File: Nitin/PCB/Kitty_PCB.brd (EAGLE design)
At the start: 384.8 x 406.1 mm, 49 parts

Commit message: PCB 1.0 Final
1st version of the PCB is completed.
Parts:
- removed C1: (no value), robocon:C050-075X075
- removed LED1, LED2, LED3, LED4, LED5: LED, robocon:LED3MM
- removed R3: (no value), robocon:0207/10
- added 5VLED, 9VLED, A1LED, A2LED: LED, robocon:LED3MM
- moved SCREW_TERMINAL2 378.1 mm to (19.1, 0.00), turned to 0 degrees
- moved SCREW_TERMINAL_1 346.6 mm to (38.1, 0.00), turned to 0 degrees
- moved ENCODER6 296.1 mm to (38.1, -35.6), turned to 270 degrees
- moved MOSFET 291.7 mm to (47.0, -14.0), turned to 0 degrees
- moved ENCODER5 291.7 mm to (38.1, -73.7), turned to 270 degrees
- moved R2 281.3 mm to (57.1, -61.0), turned to 90 degrees
- moved 7809 278.8 mm to (10.2, -95.2), turned to 270 degrees
- moved 7809B 268.3 mm to (26.7, -95.2), turned to 270 degrees
- moved MD1 244.1 mm to (62.2, -250.2)
- moved R4 224.8 mm to (61.2, -227.3), turned to 180 degrees
- moved MD3 220.6 mm to (62.2, -5.08), turned to 180 degrees
- moved ENCODER2 200.3 mm to (188.0, -176.5)
- moved SV17 198.8 mm to (74.4, -212.1)
- moved SV4 189.8 mm to (74.4, -168.9)
- moved SV5 189.8 mm to (74.4, -191.8)
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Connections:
- removed net N$115: LED3.K, R3.1
- new net N$8: A2LED.A, R5.2
- net 12V_OUT: no longer C1.1, LED3.A
- net GND: now also 5VLED.K, 9VLED.K, A1LED.K, A2LED.K; no longer C1.2, LED1.K, LED2.K, LED4.K, LED5.A, LED5.K, R3.2, R5.2
- net N$19: now also 9VLED.A; no longer LED2.A
- net N$3: now also 5VLED.A; no longer LED1.A
- net N$7: now also A1LED.A; no longer LED4.A
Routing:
- net 5V: track 0.00 -> 791.0 mm, vias 0 -> 3
- net 9V: track 0.00 -> 478.5 mm, vias 0 -> 2
- net GND: track 0.00 -> 360.7 mm, vias 0 -> 9
- net 9A2: track 0.00 -> 347.3 mm, vias 0 -> 2
- net A1SC2: track 0.00 -> 245.8 mm
- net 23A2: track 0.00 -> 204.0 mm
- net 12V_OUT: track 0.00 -> 199.7 mm
- net 25A2: track 0.00 -> 197.4 mm
- net 27A1: track 0.00 -> 189.7 mm, vias 0 -> 1
- net 23A1: track 0.00 -> 186.3 mm
- net 25A1: track 0.00 -> 180.0 mm, vias 0 -> 1
- net 29A2: track 0.00 -> 177.2 mm
- net 27A2: track 0.00 -> 167.8 mm
- net 5A1: track 0.00 -> 165.8 mm
- net 18A2: track 0.00 -> 149.9 mm, vias 0 -> 1
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- added copper zone on layer 1, net GND
- added copper zone on layer 16, net GND
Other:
- board size 384.8 x 406.1 mm -> 204.4 x 284.1 mm
- board text added: "9V"
- board text added: "E6"
- board text added: "KITTY 1.0"
- board text added: "MaRS IITR"

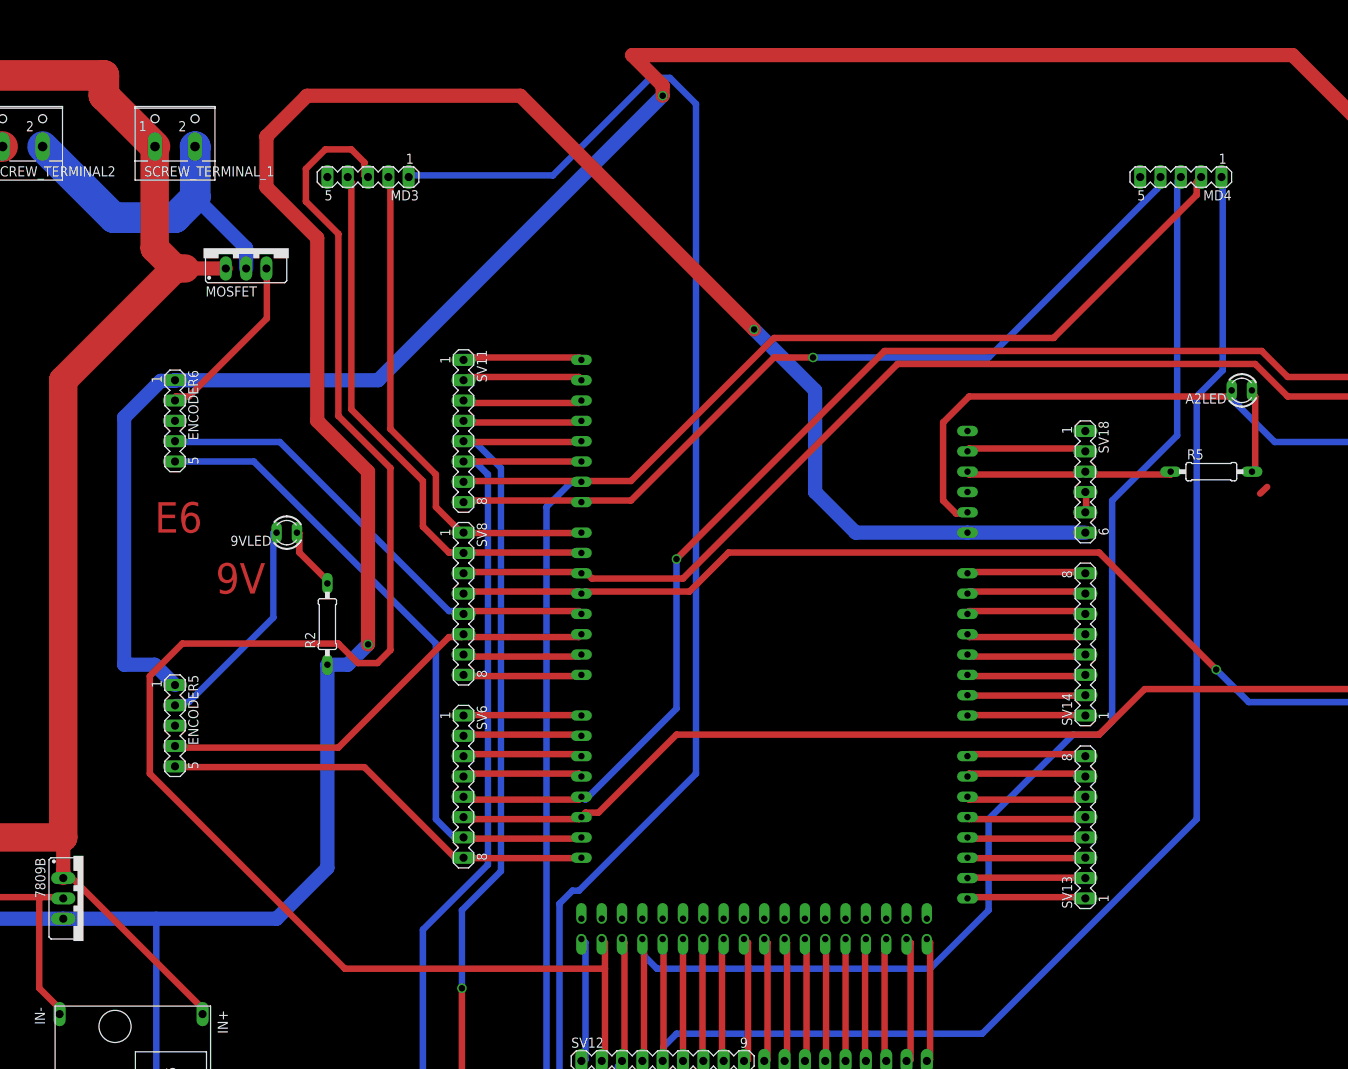
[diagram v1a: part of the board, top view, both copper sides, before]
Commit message: New Things To be Added
Integrating IMU for COM position
Storing value in EEPROM of Arduino for repositioning off the bot each time it starts.
Adding Spline to the motion of 1leg.
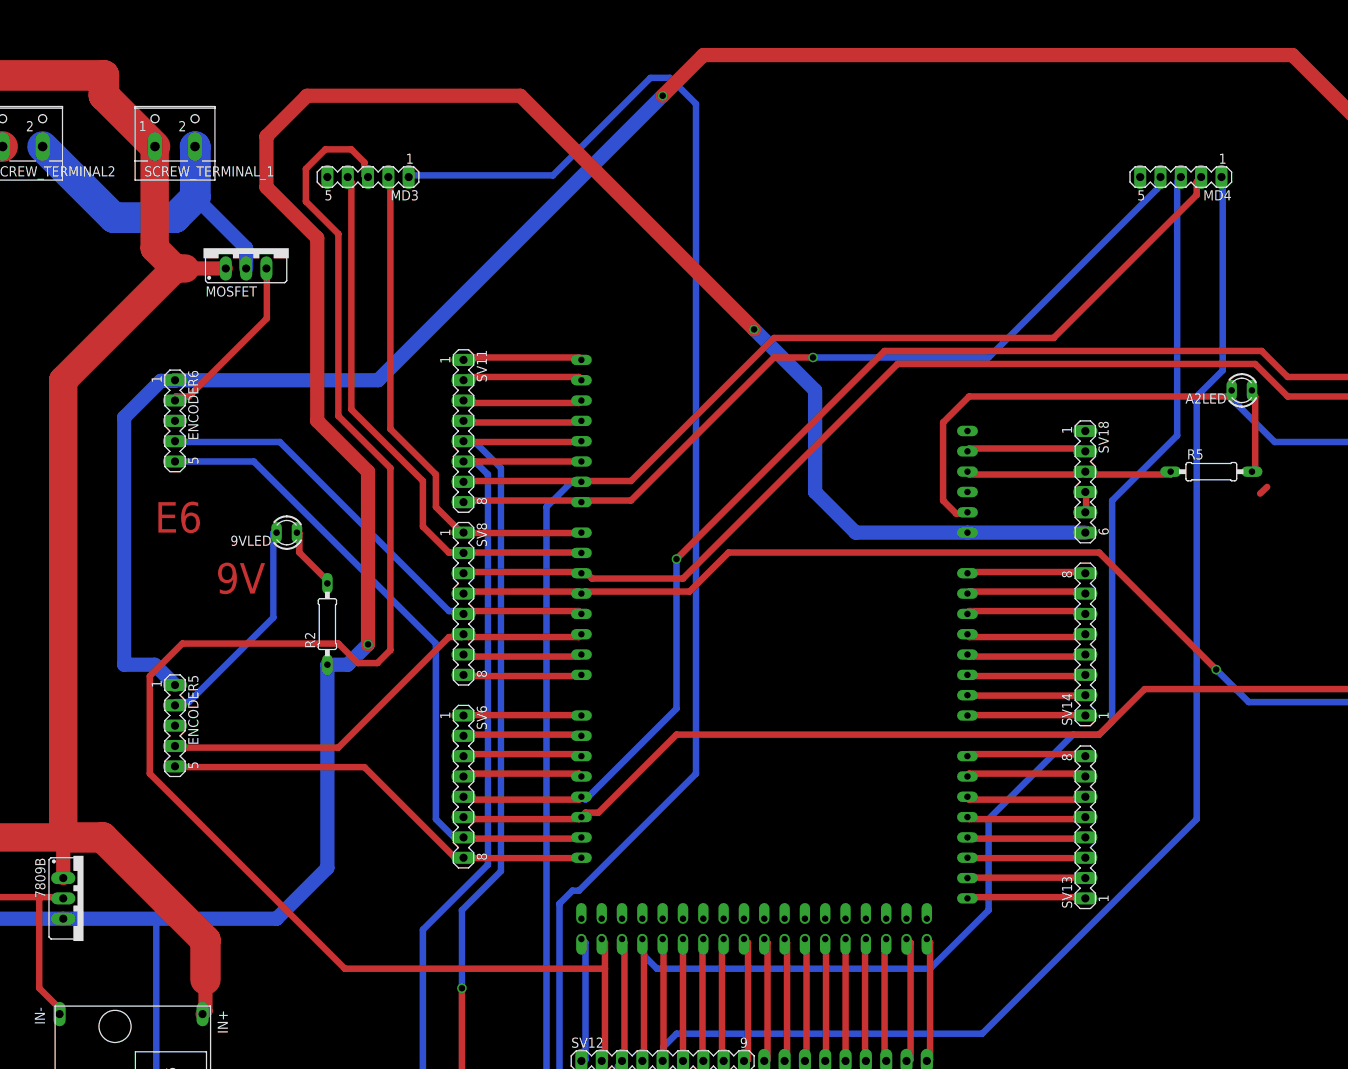
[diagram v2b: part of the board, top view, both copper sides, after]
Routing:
- net 5V: track 791.0 -> 782.7 mm
- net 12V_OUT: track 199.7 -> 207.0 mm
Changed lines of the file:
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@@
 <drawing>
 <settings>
-<setting alwaysvectorfont="yes"/>
+<setting alwaysvectorfont="no"/>
 <setting verticaltext="up"/>
 </settings>
@@
 <wire x1="193.04" y1="-45.72" x2="193.04" y2="-5.08" width="1.778" layer="1"/>
 <wire x1="193.04" y1="-5.08" x2="177.8" y2="10.16" width="1.778" layer="1"/>
-<wire x1="177.8" y1="10.16" x2="95.25" y2="10.16" width="1.778" layer="1"/>
-<wire x1="95.25" y1="10.16" x2="99.06" y2="6.35" width="1.778" layer="1"/>
-<wire x1="99.06" y1="6.35" x2="99.06" y2="5.08" width="1.778" layer="1"/>
+<wire x1="177.8" y1="10.16" x2="104.14" y2="10.16" width="1.778" layer="1"/>
+<wire x1="104.14" y1="10.16" x2="99.06" y2="5.08" width="1.778" layer="1"/>
 <via x="99.06" y="5.08" extent="1-16" drill="0.8128"/>
 <wire x1="99.06" y1="5.08" x2="63.5" y2="-30.48" width="1.778" layer="16"/>
@@
 <wire x1="24.13" y1="-87.63" x2="7.62" y2="-87.63" width="3.556" layer="1"/>
 <wire x1="7.62" y1="-87.63" x2="7.62" y2="-92.71" width="1.778" layer="1"/>
-<wire x1="24.13" y1="-87.63" x2="24.13" y2="-91.8464" width="1.778" layer="1"/>
-<wire x1="24.13" y1="-91.8464" x2="24.13" y2="-92.71" width="1.778" layer="1"/>
-<wire x1="24.384" y1="-91.8464" x2="41.4528" y2="-108.9152" width="0.8128" layer="1"/>
-<wire x1="41.4528" y1="-108.9152" x2="41.545" y2="-109.712" width="0.8128" layer="1"/>
-<wire x1="24.384" y1="-91.8464" x2="24.13" y2="-91.8464" width="0.8128" layer="1"/>
+<wire x1="24.13" y1="-87.63" x2="24.13" y2="-92.71" width="1.778" layer="1"/>
+<wire x1="24.13" y1="-87.63" x2="29.0576" y2="-87.63" width="3.81" layer="1"/>
+<wire x1="29.0576" y1="-87.63" x2="41.91" y2="-100.4824" width="3.81" layer="1"/>
+<wire x1="41.91" y1="-100.4824" x2="41.91" y2="-105.41" width="3.81" layer="1"/>
+<wire x1="41.91" y1="-105.41" x2="41.91" y2="-109.347" width="1.778" layer="1"/>
+<wire x1="41.91" y1="-109.347" x2="41.545" y2="-109.712" width="1.778" layer="1"/>
 </signal>
 <signal name="12V_IN_GND">
